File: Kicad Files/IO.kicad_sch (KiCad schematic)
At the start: 1 part, among them U67 RP2040

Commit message: tidy up
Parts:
- renumbered U67 to U46
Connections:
- net at U46.1 (IOVDD), U46.10 (IOVDD), U46.22 (IOVDD)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: now also U46.23 (DVDD), U46.50 (DVDD)
- no-connect marks 21 -> 19
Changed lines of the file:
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@@
   (no_connect (at 121.285 97.155))
   (no_connect (at 93.345 97.155))
-  (no_connect (at 85.725 74.295))
   (no_connect (at 85.725 76.835))
-  (no_connect (at 85.725 69.215))
   (no_connect (at 85.725 66.675))
   (no_connect (at 85.725 64.135))
@@
   (no_connect (at 161.925 46.355))
   (no_connect (at 164.465 46.355))
+  (wire (pts (xy 85.725 69.215) (xy 85.725 74.295))
+    (stroke (width 0) (type default) (color 0 0 0 0))
+  )
   (hierarchical_label "BUS_7" (shape bidirectional) (at 116.205 46.355 90)
     (effects (font (size 1.524 1.524)) (justify left))
@@
   (symbol (lib_id "MCU_RaspberryPi:RP2040") (at 131.445 71.755 90) (unit 1)
     (in_bom yes) (on_board yes) (fields_autoplaced)
-    (property "Reference" "U67" (id 0) (at 179.07 68.1736 90))
+    (property "Reference" "U46" (id 0) (at 179.07 68.1736 90))
     (property "Value" "RP2040" (id 1) (at 179.07 70.7136 90))
     (property "Footprint" "Package_DFN_QFN:QFN-56-1EP_7x7mm_P0.4mm_EP3.2x3.2mm" (id 2) (at 131.445 71.755 0)
@@
   (symbol (lib_id "power:VCC") (at 85.725 61.595 0) (unit 1)
     (in_bom yes) (on_board yes) (fields_autoplaced)
-    (property "Reference" "#PWR0132" (id 0) (at 85.725 65.405 0)
+    (property "Reference" "#PWR0114" (id 0) (at 85.725 65.405 0)
       (effects (font (size 1.27 1.27)) hide)
     )
@@
   (symbol (lib_id "power:GND") (at 177.165 71.755 0) (unit 1)
     (in_bom yes) (on_board yes) (fields_autoplaced)
-    (property "Reference" "#PWR0133" (id 0) (at 177.165 78.105 0)
+    (property "Reference" "#PWR0115" (id 0) (at 177.165 78.105 0)
       (effects (font (size 1.27 1.27)) hide)
     )

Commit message: updated library
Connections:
- net HLT: now reaches U46.39 (GPIO27_ADC1)
- no-connect marks 19 -> 18
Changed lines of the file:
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@@
   (no_connect (at 139.065 97.155))
   (no_connect (at 161.925 46.355))
-  (no_connect (at 164.465 46.355))
   (wire (pts (xy 85.725 69.215) (xy 85.725 74.295))
     (stroke (width 0) (type default) (color 0 0 0 0))
@@
     (effects (font (size 1.524 1.524)) (justify left))
   )
+  (hierarchical_label "HLT" (shape tri_state) (at 164.465 46.355 90)
+    (effects (font (size 1.524 1.524)) (justify left))
+  )
   (hierarchical_label "ABUS_00" (shape tri_state) (at 156.845 46.355 90)
     (effects (font (size 1.524 1.524)) (justify left))
   )
-  (hierarchical_label "CLR" (shape output) (at 169.545 46.355 90)
+  (hierarchical_label "CLR" (shape tri_state) (at 169.545 46.355 90)
     (effects (font (size 1.524 1.524)) (justify left))
   )
@@
     (effects (font (size 1.524 1.524)) (justify left))
   )
-  (hierarchical_label "OVRD" (shape output) (at 167.005 46.355 90)
+  (hierarchical_label "OVRD" (shape tri_state) (at 167.005 46.355 90)
     (effects (font (size 1.524 1.524)) (justify left))
   )
@@
   (symbol (lib_id "power:VCC") (at 85.725 61.595 0) (unit 1)
     (in_bom yes) (on_board yes) (fields_autoplaced)
-    (property "Reference" "#PWR0114" (id 0) (at 85.725 65.405 0)
+    (property "Reference" "#PWR0151" (id 0) (at 85.725 65.405 0)
       (effects (font (size 1.27 1.27)) hide)
     )
@@
   (symbol (lib_id "power:GND") (at 177.165 71.755 0) (unit 1)
     (in_bom yes) (on_board yes) (fields_autoplaced)
-    (property "Reference" "#PWR0115" (id 0) (at 177.165 78.105 0)
+    (property "Reference" "#PWR0152" (id 0) (at 177.165 78.105 0)
       (effects (font (size 1.27 1.27)) hide)
     )

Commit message: work on clk
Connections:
- net ~{CLK}: now reaches U46.38 (GPIO26_ADC0)
- no-connect marks 18 -> 17
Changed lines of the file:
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@@
   (no_connect (at 169.545 97.155))
   (no_connect (at 139.065 97.155))
-  (no_connect (at 161.925 46.355))
   (wire (pts (xy 85.725 69.215) (xy 85.725 74.295))
     (stroke (width 0) (type default) (color 0 0 0 0))
@@
     (effects (font (size 1.524 1.524)) (justify left))
   )
+  (hierarchical_label "~{CLK}" (shape tri_state) (at 161.925 46.355 90)
+    (effects (font (size 1.524 1.524)) (justify left))
+  )

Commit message: im sooo stupiiid
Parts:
- renumbered U46 to U48
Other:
- moved on the sheet: U48

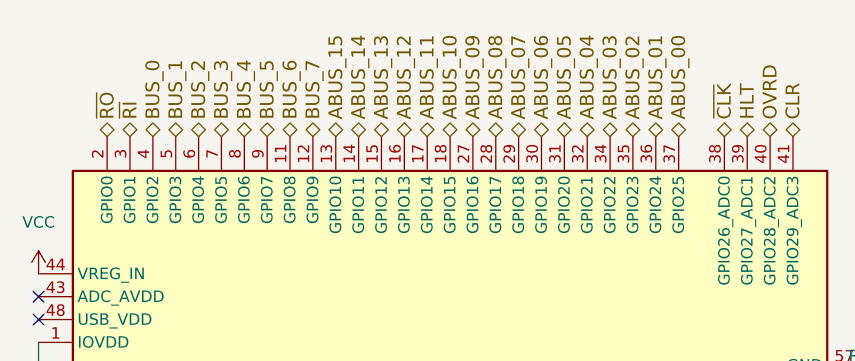
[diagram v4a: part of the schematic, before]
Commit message: complete redraw to bus system
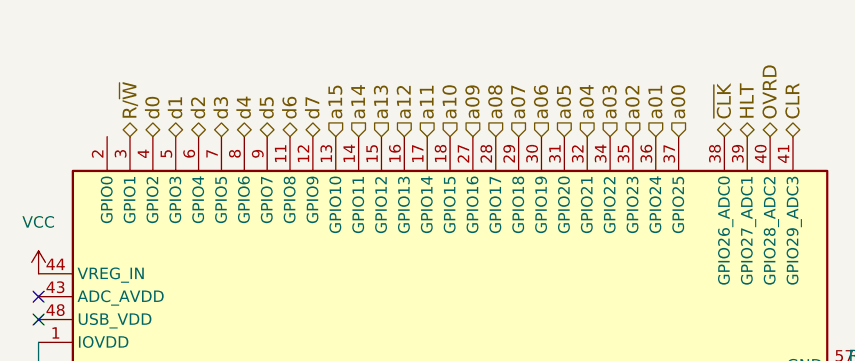
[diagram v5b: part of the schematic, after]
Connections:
- net ABUS_00 renamed a00
- net ABUS_01 renamed a01
- net ABUS_02 renamed a02
- net ABUS_03 renamed a03
- net ABUS_04 renamed a04
- net ABUS_05 renamed a05
- net ABUS_06 renamed a06
- net ABUS_07 renamed a07
- net ABUS_08 renamed a08
- net ABUS_09 renamed a09
- net ABUS_10 renamed a10
- net ABUS_11 renamed a11
- net ABUS_12 renamed a12
- net ABUS_13 renamed a13
- net ABUS_14 renamed a14
- net ABUS_15 renamed a15
- net BUS_0 renamed d0
- net BUS_1 renamed d1
- net BUS_2 renamed d2
- net BUS_3 renamed d3
- net BUS_4 renamed d4
- net BUS_5 renamed d5
- net BUS_6 renamed d6
- net BUS_7 renamed d7
- net ~{RI} renamed R/~{W}
- net ~{RO}: no longer names the net of U48.2 (GPIO0)
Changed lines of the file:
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@@
     (stroke (width 0) (type default) (color 0 0 0 0))
   )
-  (hierarchical_label "BUS_7" (shape bidirectional) (at 139.7 81.915 90)
+  (hierarchical_label "a04" (shape input) (at 170.18 81.915 90)
     (effects (font (size 1.524 1.524)) (justify left))
   )
-  (hierarchical_label "BUS_2" (shape bidirectional) (at 127 81.915 90)
+  (hierarchical_label "a11" (shape input) (at 152.4 81.915 90)
     (effects (font (size 1.524 1.524)) (justify left))
   )
-  (hierarchical_label "BUS_4" (shape bidirectional) (at 132.08 81.915 90)
+  (hierarchical_label "d6" (shape tri_state) (at 137.16 81.915 90)
     (effects (font (size 1.524 1.524)) (justify left))
   )
-  (hierarchical_label "ABUS_02" (shape tri_state) (at 175.26 81.915 90)
+  (hierarchical_label "R{slash}~{W}" (shape tri_state) (at 119.38 81.915 90)
     (effects (font (size 1.524 1.524)) (justify left))
   )
-  (hierarchical_label "ABUS_03" (shape tri_state) (at 172.72 81.915 90)
+  (hierarchical_label "a10" (shape input) (at 154.94 81.915 90)
     (effects (font (size 1.524 1.524)) (justify left))
   )
-  (hierarchical_label "BUS_3" (shape bidirectional) (at 129.54 81.915 90)
-    (effects (font (size 1.524 1.524)) (justify left))
-  )
-  (hierarchical_label "ABUS_15" (shape tri_state) (at 142.24 81.915 90)
-    (effects (font (size 1.524 1.524)) (justify left))
-  )
-  (hierarchical_label "ABUS_10" (shape tri_state) (at 154.94 81.915 90)
-    (effects (font (size 1.524 1.524)) (justify left))
-  )
-  (hierarchical_label "BUS_6" (shape bidirectional) (at 137.16 81.915 90)
+  (hierarchical_label "a14" (shape input) (at 144.78 81.915 90)
     (effects (font (size 1.524 1.524)) (justify left))
   )
@@
     (effects (font (size 1.524 1.524)) (justify left))
   )
-  (hierarchical_label "ABUS_00" (shape tri_state) (at 180.34 81.915 90)
+  (hierarchical_label "a07" (shape input) (at 162.56 81.915 90)
     (effects (font (size 1.524 1.524)) (justify left))
   )
@@
     (effects (font (size 1.524 1.524)) (justify left))
   )
+  (hierarchical_label "a12" (shape input) (at 149.86 81.915 90)
+    (effects (font (size 1.524 1.524)) (justify left))
+  )
   (hierarchical_label "CLR" (shape tri_state) (at 193.04 81.915 90)
     (effects (font (size 1.524 1.524)) (justify left))
   )
-  (hierarchical_label "BUS_5" (shape bidirectional) (at 134.62 81.915 90)
+  (hierarchical_label "a01" (shape input) (at 177.8 81.915 90)
     (effects (font (size 1.524 1.524)) (justify left))
   )
-  (hierarchical_label "ABUS_01" (shape tri_state) (at 177.8 81.915 90)
+  (hierarchical_label "a15" (shape input) (at 142.24 81.915 90)
     (effects (font (size 1.524 1.524)) (justify left))
   )
-  (hierarchical_label "BUS_1" (shape bidirectional) (at 124.46 81.915 90)
+  (hierarchical_label "d0" (shape tri_state) (at 121.92 81.915 90)
     (effects (font (size 1.524 1.524)) (justify left))
   )
-  (hierarchical_label "ABUS_08" (shape tri_state) (at 160.02 81.915 90)
+  (hierarchical_label "a03" (shape input) (at 172.72 81.915 90)
     (effects (font (size 1.524 1.524)) (justify left))
   )
-  (hierarchical_label "ABUS_12" (shape tri_state) (at 149.86 81.915 90)
+  (hierarchical_label "d5" (shape tri_state) (at 134.62 81.915 90)
+    (effects (font (size 1.524 1.524)) (justify left))
+  )
+  (hierarchical_label "a09" (shape input) (at 157.48 81.915 90)
     (effects (font (size 1.524 1.524)) (justify left))
   )
@@
     (effects (font (size 1.524 1.524)) (justify left))
   )
-  (hierarchical_label "ABUS_13" (shape tri_state) (at 147.32 81.915 90)
+  (hierarchical_label "d7" (shape tri_state) (at 139.7 81.915 90)
     (effects (font (size 1.524 1.524)) (justify left))
   )
-  (hierarchical_label "ABUS_07" (shape tri_state) (at 162.56 81.915 90)
+  (hierarchical_label "a05" (shape input) (at 167.64 81.915 90)
     (effects (font (size 1.524 1.524)) (justify left))
   )
-  (hierarchical_label "ABUS_05" (shape tri_state) (at 167.64 81.915 90)
+  (hierarchical_label "a02" (shape input) (at 175.26 81.915 90)
     (effects (font (size 1.524 1.524)) (justify left))
   )
-  (hierarchical_label "ABUS_04" (shape tri_state) (at 170.18 81.915 90)
+  (hierarchical_label "d1" (shape tri_state) (at 124.46 81.915 90)
     (effects (font (size 1.524 1.524)) (justify left))
   )
-  (hierarchical_label "ABUS_11" (shape tri_state) (at 152.4 81.915 90)
+  (hierarchical_label "d3" (shape tri_state) (at 129.54 81.915 90)
     (effects (font (size 1.524 1.524)) (justify left))
   )
-  (hierarchical_label "~{RI}" (shape tri_state) (at 119.38 81.915 90)
+  (hierarchical_label "a13" (shape input) (at 147.32 81.915 90)
     (effects (font (size 1.524 1.524)) (justify left))
   )
-  (hierarchical_label "~{RO}" (shape tri_state) (at 116.84 81.915 90)
+  (hierarchical_label "a00" (shape input) (at 180.34 81.915 90)
     (effects (font (size 1.524 1.524)) (justify left))
   )
-  (hierarchical_label "ABUS_09" (shape tri_state) (at 157.48 81.915 90)
+  (hierarchical_label "d2" (shape tri_state) (at 127 81.915 90)
     (effects (font (size 1.524 1.524)) (justify left))
   )
-  (hierarchical_label "BUS_0" (shape bidirectional) (at 121.92 81.915 90)
+  (hierarchical_label "a06" (shape input) (at 165.1 81.915 90)
     (effects (font (size 1.524 1.524)) (justify left))
   )
-  (hierarchical_label "ABUS_06" (shape tri_state) (at 165.1 81.915 90)
+  (hierarchical_label "a08" (shape input) (at 160.02 81.915 90)
     (effects (font (size 1.524 1.524)) (justify left))
   )
-  (hierarchical_label "ABUS_14" (shape tri_state) (at 144.78 81.915 90)
+  (hierarchical_label "d4" (shape tri_state) (at 132.08 81.915 90)
     (effects (font (size 1.524 1.524)) (justify left))
   )

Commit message: update
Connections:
- net CLR: no longer names the net of U48.41 (GPIO29_ADC3)
- net HLT: no longer names the net of U48.39 (GPIO27_ADC1)
- net OVRD: no longer names the net of U48.40 (GPIO28_ADC2)
- net d0 renamed d_{e}0
- net d1 renamed d_{e}1
- net d2 renamed d_{e}2
- net d3 renamed d_{e}3
- net d4 renamed d_{e}4
- net d5 renamed d_{e}5
- net d6 renamed d_{e}6
- net d7 renamed d_{e}7
- net ~{CLK}: no longer names the net of U48.38 (GPIO26_ADC0)
